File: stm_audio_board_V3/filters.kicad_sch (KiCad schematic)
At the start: 29 parts

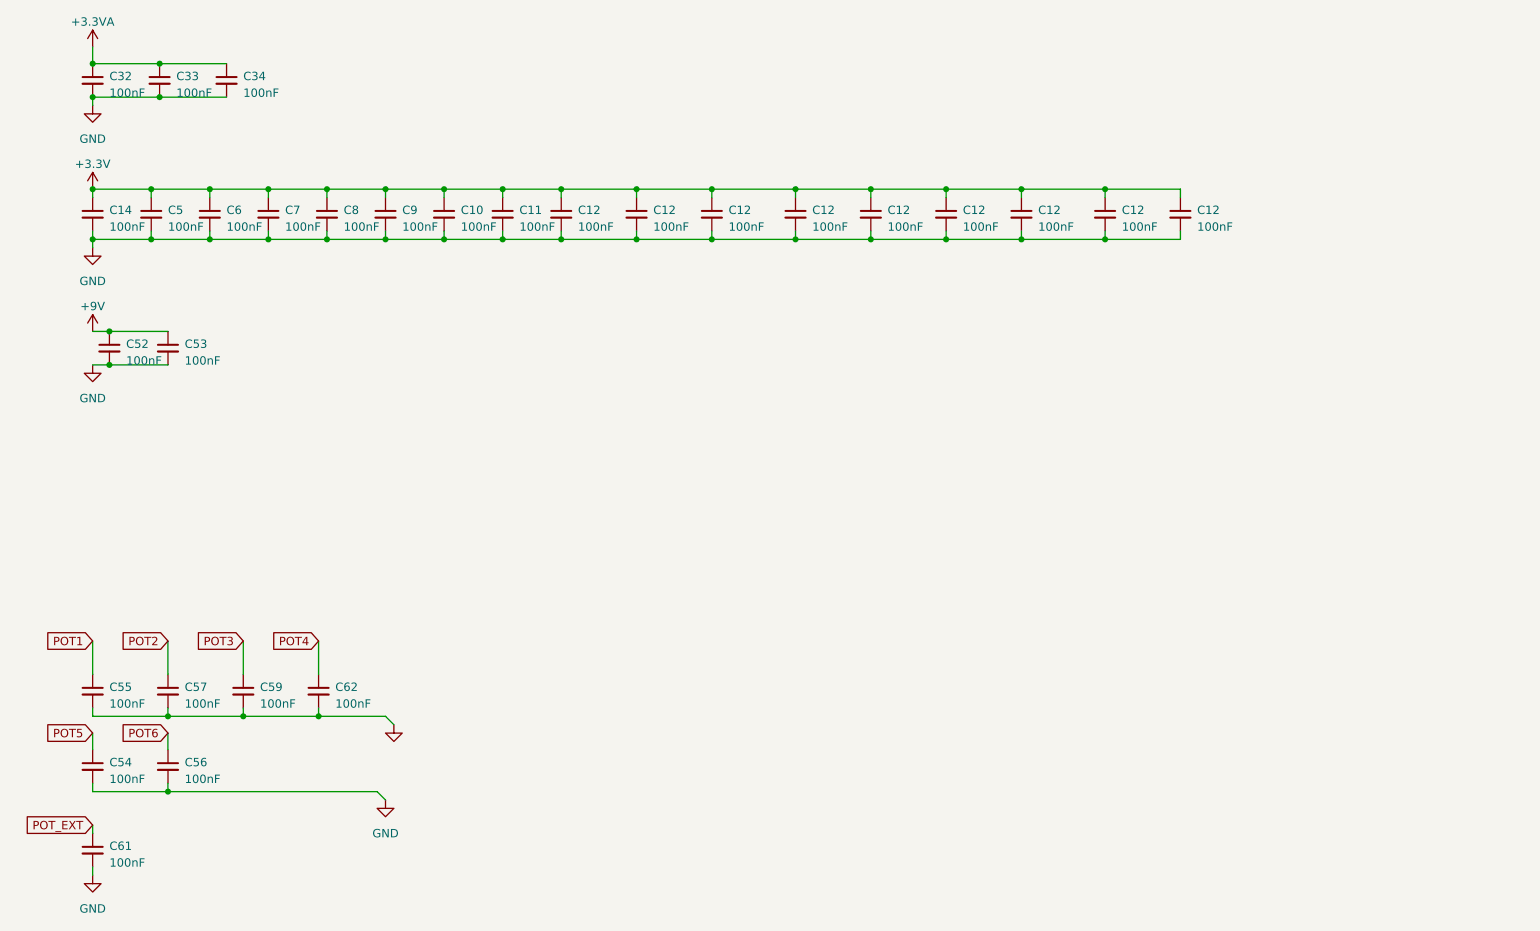
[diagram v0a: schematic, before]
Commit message: Input and output stages are made and assembly started on pcb view
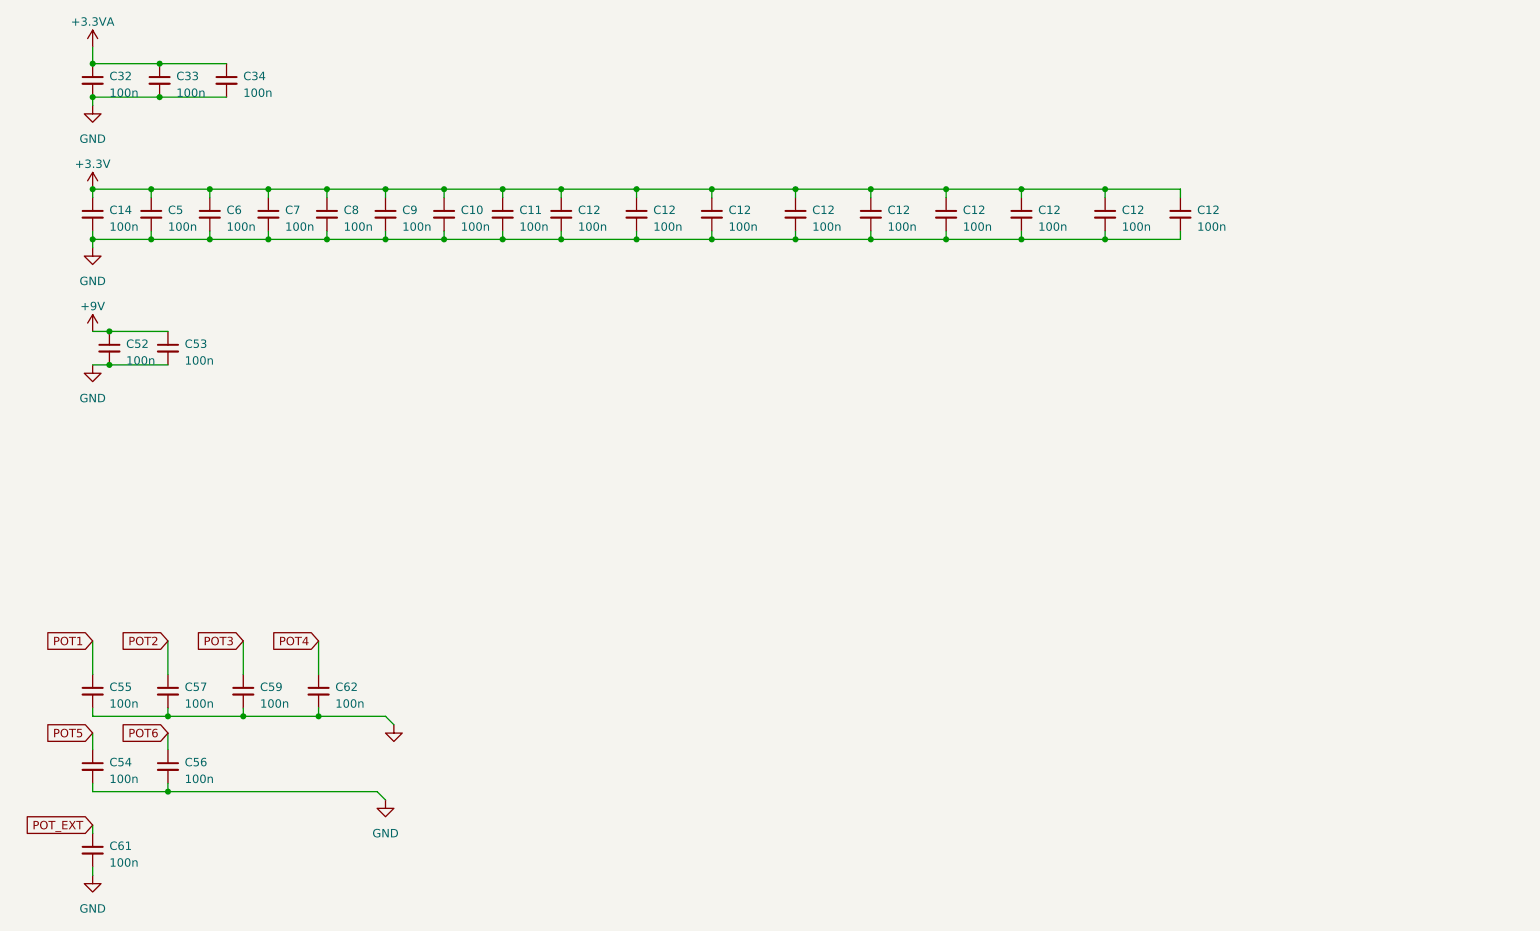
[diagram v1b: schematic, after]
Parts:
- C10, C11, C12, C14, C32, C33, C34, C5, C52, C53, C54, C55, C56, C57, C59, C6, C61, C62, C7, C8, C9: value 100nF -> 100n; footprint Capacitor_SMD:C_0603_1608Metric_Pad1.08x0.95mm_HandSolder -> Capacitor_SMD:C_0603_1608Metric

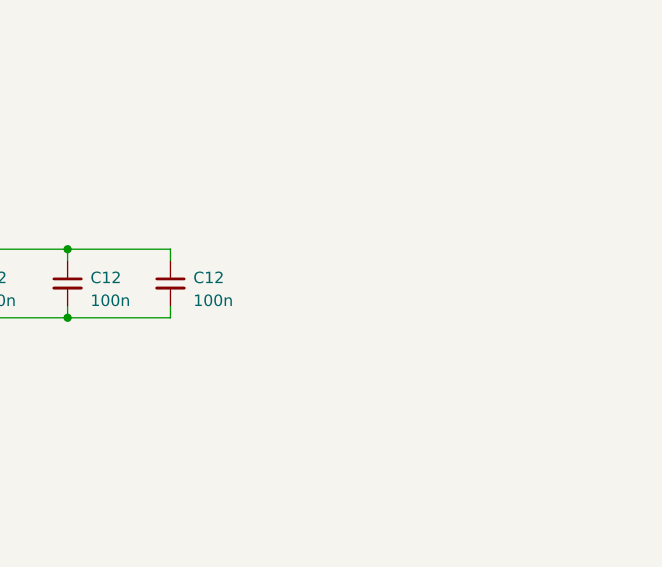
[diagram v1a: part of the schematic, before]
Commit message: Footswitch debounce added
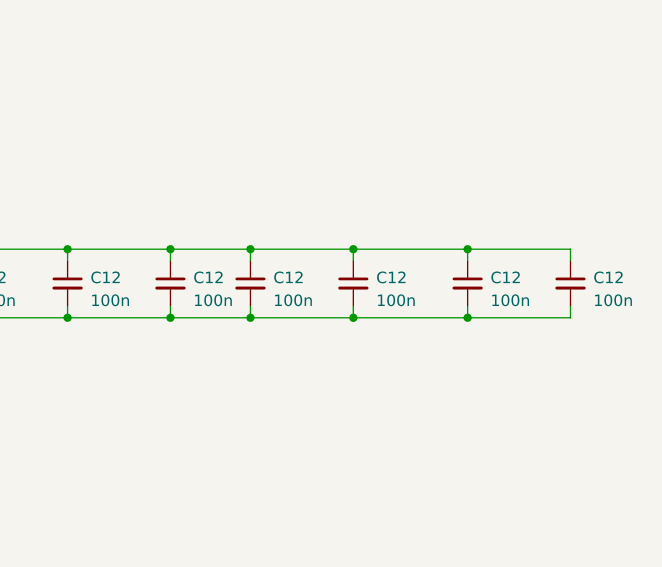
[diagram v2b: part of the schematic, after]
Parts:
- added C12 (x4): 100n, Capacitor_SMD:C_0603_1608Metric, symbol Device:C_Small
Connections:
- net +3.3V: now also C12.1, C12.1, C12.1, C12.1
- net GND: now also C12.2, C12.2, C12.2, C12.2
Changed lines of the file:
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@@
   (junction (at 167.64 54.61) (diameter 0) (color 0 0 0 0)
   )
+  (junction (at 224.79 46.99) (diameter 0) (color 0 0 0 0)
+  )
+  (junction (at 212.09 46.99) (diameter 0) (color 0 0 0 0)
+  )
+  (junction (at 191.77 54.61) (diameter 0) (color 0 0 0 0)
+  )
   (junction (at 35.56 46.99) (diameter 0) (color 0 0 0 0)
   )
@@
   (junction (at 60.96 127) (diameter 0) (color 0 0 0 0)
   )
+  (junction (at 200.66 54.61) (diameter 0) (color 0 0 0 0)
+  )
   (junction (at 88.9 46.99) (diameter 0) (color 0 0 0 0)
   )
   (junction (at 167.64 46.99) (diameter 0) (color 0 0 0 0)
   )
+  (junction (at 212.09 54.61) (diameter 0) (color 0 0 0 0)
+  )
   (junction (at 71.12 54.61) (diameter 0) (color 0 0 0 0)
   )
@@
   (junction (at 53.34 46.99) (diameter 0) (color 0 0 0 0)
   )
+  (junction (at 224.79 54.61) (diameter 0) (color 0 0 0 0)
+  )
   (junction (at 35.56 54.61) (diameter 0) (color 0 0 0 0)
   )
@@
   (junction (at 38.1 127) (diameter 0) (color 0 0 0 0)
   )
+  (junction (at 191.77 46.99) (diameter 0) (color 0 0 0 0)
+  )
   (junction (at 97.79 46.99) (diameter 0) (color 0 0 0 0)
   )
@@
   (junction (at 26.67 54.61) (diameter 0) (color 0 0 0 0)
   )
+  (junction (at 200.66 46.99) (diameter 0) (color 0 0 0 0)
+  )
   (junction (at 88.9 54.61) (diameter 0) (color 0 0 0 0)
   )
@@
     (stroke (width 0) (type default))
   )
+  (wire (pts (xy 236.22 53.34) (xy 236.22 54.61))
+    (stroke (width 0) (type default))
+  )
+  (wire (pts (xy 191.77 46.99) (xy 200.66 46.99))
+    (stroke (width 0) (type default))
+  )
   (wire (pts (xy 62.23 54.61) (xy 53.34 54.61))
     (stroke (width 0) (type default))
@@
     (stroke (width 0) (type default))
   )
+  (wire (pts (xy 200.66 53.34) (xy 200.66 54.61))
+    (stroke (width 0) (type default))
+  )
   (wire (pts (xy 53.34 46.99) (xy 62.23 46.99))
     (stroke (width 0) (type default))
@@
     (stroke (width 0) (type default))
   )
+  (wire (pts (xy 224.79 54.61) (xy 236.22 54.61))
+    (stroke (width 0) (type default))
+  )
   (wire (pts (xy 60.96 115.57) (xy 60.96 120.65))
     (stroke (width 0) (type default))
   )
+  (wire (pts (xy 212.09 46.99) (xy 200.66 46.99))
+    (stroke (width 0) (type default))
+  )
   (wire (pts (xy 62.23 46.99) (xy 71.12 46.99))
     (stroke (width 0) (type default))
@@
     (stroke (width 0) (type default))
   )
+  (wire (pts (xy 212.09 54.61) (xy 224.79 54.61))
+    (stroke (width 0) (type default))
+  )
   (wire (pts (xy 62.23 48.26) (xy 62.23 46.99))
     (stroke (width 0) (type default))
   )
+  (wire (pts (xy 200.66 54.61) (xy 212.09 54.61))
+    (stroke (width 0) (type default))
+  )
   (wire (pts (xy 71.12 53.34) (xy 71.12 54.61))
     (stroke (width 0) (type default))
@@
     (stroke (width 0) (type default))
   )
+  (wire (pts (xy 224.79 53.34) (xy 224.79 54.61))
+    (stroke (width 0) (type default))
+  )
   (wire (pts (xy 71.12 127) (xy 72.39 128.27))
     (stroke (width 0) (type default))
@@
     (stroke (width 0) (type default))
   )
+  (wire (pts (xy 224.79 46.99) (xy 212.09 46.99))
+    (stroke (width 0) (type default))
+  )
   (wire (pts (xy 133.35 54.61) (xy 120.65 54.61))
     (stroke (width 0) (type default))
@@
     (stroke (width 0) (type default))
   )
+  (wire (pts (xy 236.22 46.99) (xy 224.79 46.99))
+    (stroke (width 0) (type default))
+  )
   (wire (pts (xy 26.67 27.94) (xy 36.83 27.94))
     (stroke (width 0) (type default))
@@
     (stroke (width 0) (type default))
   )
+  (wire (pts (xy 236.22 48.26) (xy 236.22 46.99))
+    (stroke (width 0) (type default))
+  )
   (wire (pts (xy 97.79 54.61) (xy 109.22 54.61))
     (stroke (width 0) (type default))
@@
     (stroke (width 0) (type default))
   )
+  (wire (pts (xy 191.77 54.61) (xy 200.66 54.61))
+    (stroke (width 0) (type default))
+  )
+  (wire (pts (xy 212.09 48.26) (xy 212.09 46.99))
+    (stroke (width 0) (type default))
+  )
   (wire (pts (xy 156.21 46.99) (xy 144.78 46.99))
     (stroke (width 0) (type default))
@@
     (stroke (width 0) (type default))
   )
+  (wire (pts (xy 224.79 48.26) (xy 224.79 46.99))
+    (stroke (width 0) (type default))
+  )
   (wire (pts (xy 180.34 54.61) (xy 191.77 54.61))
     (stroke (width 0) (type default))
@@
     (stroke (width 0) (type default))
   )
+  (wire (pts (xy 200.66 48.26) (xy 200.66 46.99))
+    (stroke (width 0) (type default))
+  )
   (wire (pts (xy 26.67 138.43) (xy 38.1 138.43))
+    (stroke (width 0) (type default))
+  )
+  (wire (pts (xy 212.09 53.34) (xy 212.09 54.61))
     (stroke (width 0) (type default))
   )
@@
     )
   )
+  (symbol (lib_id "Device:C_Small") (at 236.22 50.8 0) (unit 1)
+    (in_bom yes) (on_board yes) (dnp no)
+    (property "Reference" "C12" (at 238.76 50.1713 0)
+      (effects (font (size 1.27 1.27)) (justify left))
+    )
+    (property "Value" "100n" (at 238.76 52.7113 0)
+      (effects (font (size 1.27 1.27)) (justify left))
+    )
+    (property "Footprint" "Capacitor_SMD:C_0603_1608Metric" (at 236.22 50.8 0)
+      (effects (font (size 1.27 1.27)) hide)
+    )
+    (property "Datasheet" "~" (at 236.22 50.8 0)
+      (effects (font (size 1.27 1.27)) hide)
+    )
+    (pin "1")
+    (pin "2")
+    (instances
+      (project "stm_audio_board_V3"
+        (path "/6997cf63-2615-4e49-9471-e7da1b6bae71"
+          (reference "C12") (unit 1)
+        )
+        (path "/6997cf63-2615-4e49-9471-e7da1b6bae71/927539c8-c0d0-4950-9b67-385a1cdd80f8"
+          (reference "C184") (unit 1)
+        )
+      )
+    )
+  )
   (symbol (lib_id "power:+9V") (at 26.67 68.58 0) (unit 1)
     (in_bom yes) (on_board yes) (dnp no) (fields_autoplaced)
@@
     )
   )
+  (symbol (lib_id "Device:C_Small") (at 200.66 50.8 0) (unit 1)
+    (in_bom yes) (on_board yes) (dnp no)
+    (property "Reference" "C12" (at 203.2 50.1713 0)
+      (effects (font (size 1.27 1.27)) (justify left))
+    )
+    (property "Value" "100n" (at 203.2 52.7113 0)
+      (effects (font (size 1.27 1.27)) (justify left))
+    )
+    (property "Footprint" "Capacitor_SMD:C_0603_1608Metric" (at 200.66 50.8 0)
+      (effects (font (size 1.27 1.27)) hide)
+    )
+    (property "Datasheet" "~" (at 200.66 50.8 0)
+      (effects (font (size 1.27 1.27)) hide)
+    )
+    (pin "1")
+    (pin "2")
+    (instances
+      (project "stm_audio_board_V3"
+        (path "/6997cf63-2615-4e49-9471-e7da1b6bae71"
+          (reference "C12") (unit 1)
+        )
+        (path "/6997cf63-2615-4e49-9471-e7da1b6bae71/927539c8-c0d0-4950-9b67-385a1cdd80f8"
+          (reference "C181") (unit 1)
+        )
+      )
+    )
+  )
   (symbol (lib_id "Device:C_Small") (at 88.9 50.8 0) (unit 1)
     (in_bom yes) (on_board yes) (dnp no) (fields_autoplaced)
@@
     )
   )
+  (symbol (lib_id "Device:C_Small") (at 212.09 50.8 0) (unit 1)
+    (in_bom yes) (on_board yes) (dnp no)
+    (property "Reference" "C12" (at 214.63 50.1713 0)
+      (effects (font (size 1.27 1.27)) (justify left))
+    )
+    (property "Value" "100n" (at 214.63 52.7113 0)
+      (effects (font (size 1.27 1.27)) (justify left))
+    )
+    (property "Footprint" "Capacitor_SMD:C_0603_1608Metric" (at 212.09 50.8 0)
+      (effects (font (size 1.27 1.27)) hide)
+    )
+    (property "Datasheet" "~" (at 212.09 50.8 0)
+      (effects (font (size 1.27 1.27)) hide)
+    )
+    (pin "1")
+    (pin "2")
+    (instances
+      (project "stm_audio_board_V3"
+        (path "/6997cf63-2615-4e49-9471-e7da1b6bae71"
+          (reference "C12") (unit 1)
+        )
+        (path "/6997cf63-2615-4e49-9471-e7da1b6bae71/927539c8-c0d0-4950-9b67-385a1cdd80f8"
+          (reference "C182") (unit 1)
+        )
+      )
+    )
+  )
   (symbol (lib_id "Device:C_Small") (at 80.01 50.8 0) (unit 1)
     (in_bom yes) (on_board yes) (dnp no) (fields_autoplaced)
@@
         )
       )
+    )
+  )
+  (symbol (lib_id "Device:C_Small") (at 224.79 50.8 0) (unit 1)
+    (in_bom yes) (on_board yes) (dnp no)
+    (property "Reference" "C12" (at 227.33 50.1713 0)
+      (effects (font (size 1.27 1.27)) (justify left))
+    )
+    (property "Value" "100n" (at 227.33 52.7113 0)
+      (effects (font (size 1.27 1.27)) (justify left))
+    )
+    (property "Footprint" "Capacitor_SMD:C_0603_1608Metric" (at 224.79 50.8 0)
+      (effects (font (size 1.27 1.27)) hide)
+    )
+    (property "Datasheet" "~" (at 224.79 50.8 0)
+      (effects (font (size 1.27 1.27)) hide)
+    )
+    (pin "1")
+    (pin "2")
+    (instances
+      (project "stm_audio_board_V3"
+        (path "/6997cf63-2615-4e49-9471-e7da1b6bae71"
+          (reference "C12") (unit 1)
+        )
+        (path "/6997cf63-2615-4e49-9471-e7da1b6bae71/927539c8-c0d0-4950-9b67-385a1cdd80f8"
+          (reference "C183") (unit 1)
+        )
+      )

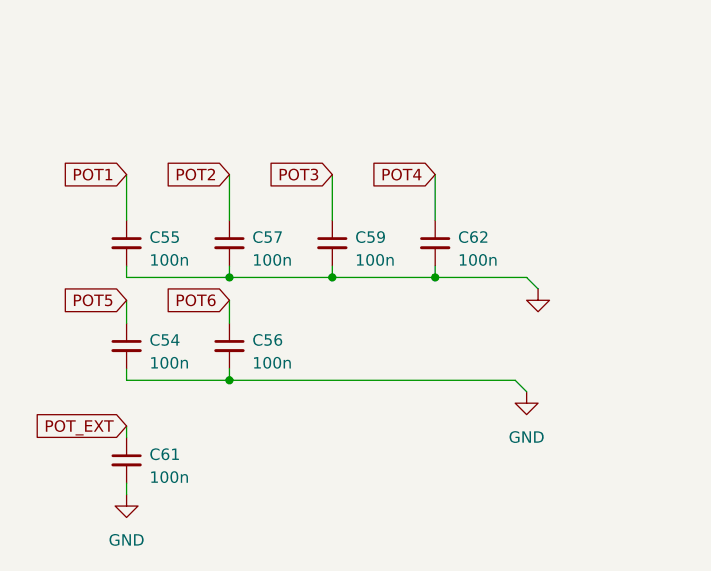
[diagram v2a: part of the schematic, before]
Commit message: New orientation, Overvoltage protection added
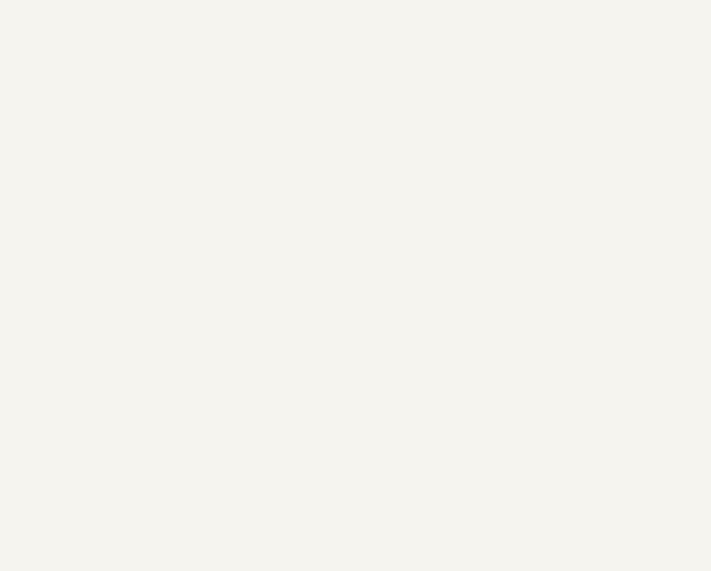
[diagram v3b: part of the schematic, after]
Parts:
- removed C54, C55, C56, C57, C59, C61, C62: 100n, Capacitor_SMD:C_0603_1608Metric, symbol Device:C_Small
